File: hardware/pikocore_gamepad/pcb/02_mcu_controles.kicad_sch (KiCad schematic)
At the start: 20 parts, among them J4 LCD_FPC, Q1 2N7002, SW1 DPAD_UP, SW10 BTN_R, SW11 BTN_START, SW12 BTN_SELECT, SW2 DPAD_DOWN, SW3 DPAD_LEFT, SW4 DPAD_RIGHT, SW5 BTN_X, SW6 BTN_Y, SW7 BTN_A, SW8 BTN_B, SW9 BTN_L, U1 RP2350-Plus-16MB

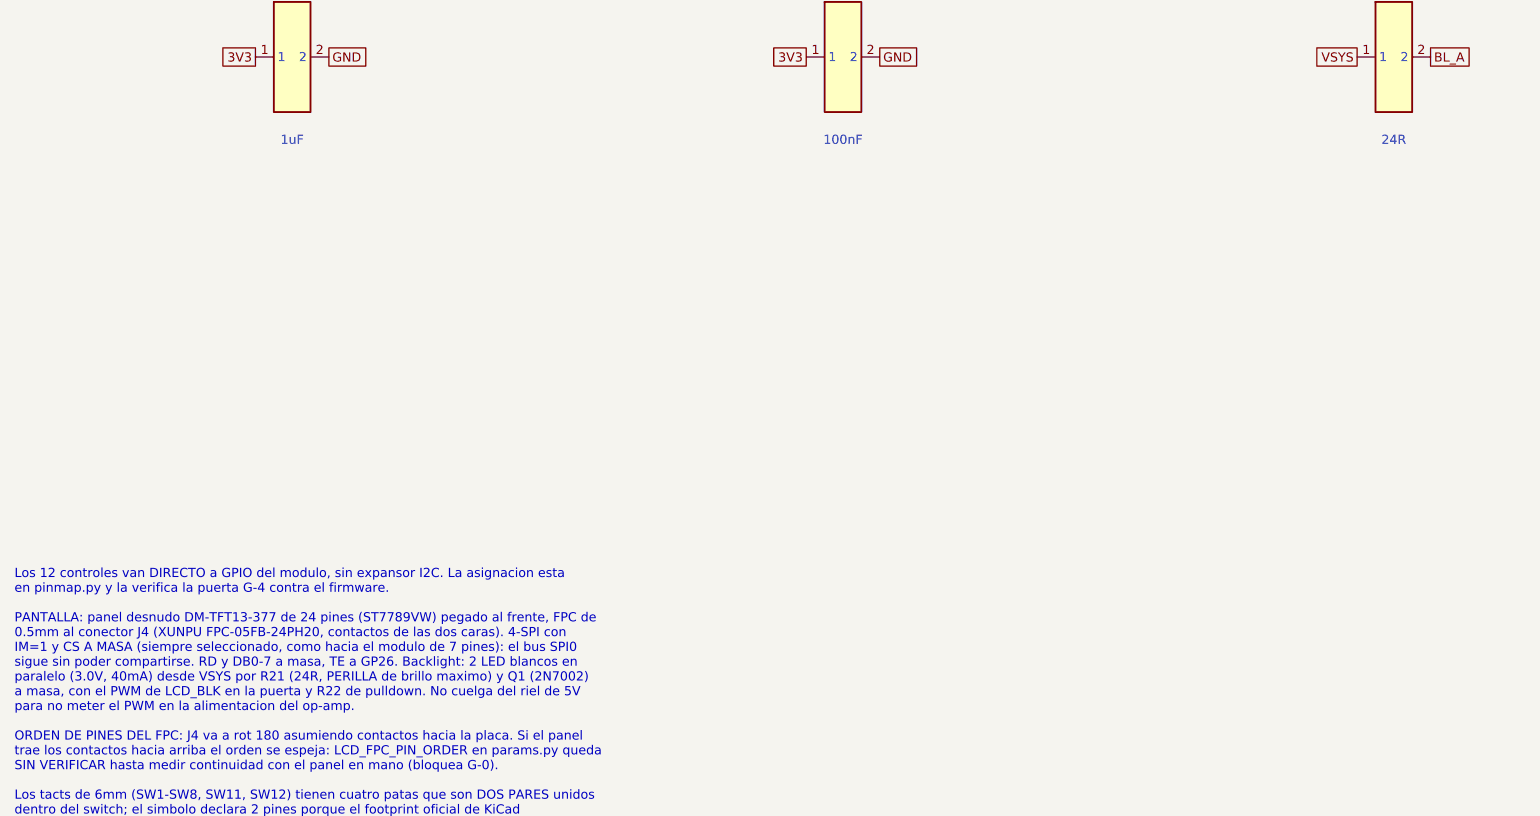
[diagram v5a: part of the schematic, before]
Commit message: hw: R21 pasa de 24R (C17576 sin stock en JLC) a 27R (C17594)
El backlight queda en 15/33/44 mA con la LiPo vacia/nominal/llena. Solo cambia
valor y codigo LCSC; el cobre no se toca (DRC 0/0/0, paridad 0).

Co-Authored-By: Claude Sonnet 5.5 <noreply@anthropic.com>
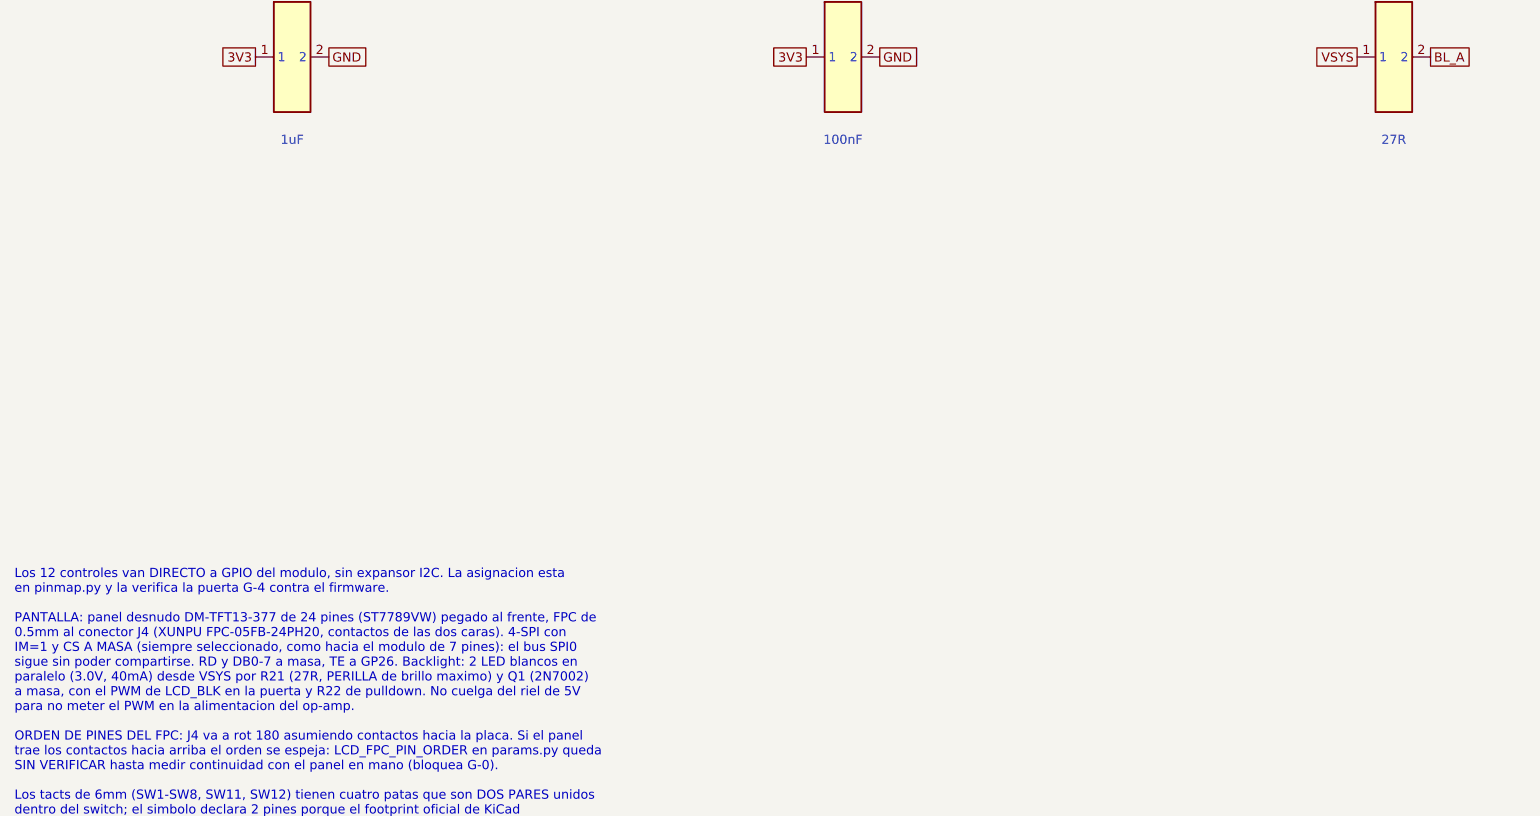
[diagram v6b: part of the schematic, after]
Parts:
- R21: value 24R -> 27R; LCSC (none) -> C17594
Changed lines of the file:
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@@
     (exclude_from_sim no) (in_bom yes) (on_board yes) (dnp no)
     (property "Reference" "R21" (at 210.82 397.51 0) (effects (font (size 1.27 1.27))))
-    (property "Value" "24R" (at 210.82 420.37 0) (effects (font (size 1.27 1.27))))
+    (property "Value" "27R" (at 210.82 420.37 0) (effects (font (size 1.27 1.27))))
     (property "Footprint" "Capacitor_SMD:C_0805_2012Metric" (at 210.82 408.94 0) (effects (font (size 1.27 1.27)) (hide yes)))
     (property "Datasheet" "" (at 210.82 408.94 0) (effects (font (size 1.27 1.27)) (hide yes)))
     (property "Description" "Resistencia SMD 0603" (at 210.82 408.94 0) (effects (font (size 1.27 1.27)) (hide yes)))
+    (property "LCSC" "C17594" (at 210.82 408.94 0) (effects (font (size 1.27 1.27)) (hide yes)))
     (pin "1")
     (pin "2")
@@
     (property "Intersheetrefs" "${INTERSHEET_REFS}" (at 292.1 408.94 0) (effects (font (size 1.27 1.27)) (hide yes)))
   )
-  (text "Los 12 controles van DIRECTO a GPIO del modulo, sin expansor I2C. La asignacion esta\nen pinmap.py y la verifica la puerta G-4 contra el firmware.\n\nPANTALLA: panel desnudo DM-TFT13-377 de 24 pines (ST7789VW) pegado al frente, FPC de\n0.5mm al conector J4 (XUNPU FPC-05FB-24PH20, contactos de las dos caras). 4-SPI con\nIM=1 y CS A MASA (siempre seleccionado, como hacia el modulo de 7 pines): el bus SPI0\nsigue sin poder compartirse. RD y DB0-7 a masa, TE a GP26. Backlight: 2 LED blancos en\nparalelo (3.0V, 40mA) desde VSYS por R21 (24R, PERILLA de brillo maximo) y Q1 (2N7002)\na masa, con el PWM de LCD_BLK en la puerta y R22 de pulldown. No cuelga del riel de 5V\npara no meter el PWM en la alimentacion del op-amp.\n\nORDEN DE PINES DEL FPC: J4 va a rot 180 asumiendo contactos hacia la placa. Si el panel\ntrae los contactos hacia arriba el orden se espeja: LCD_FPC_PIN_ORDER en params.py queda\nSIN VERIFICAR hasta medir continuidad con el panel en mano (bloquea G-0).\n\nLos tacts de 6mm (SW1-SW8, SW11, SW12) tienen cuatro patas que son DOS PARES unidos\ndentro del switch; el simbolo declara 2 pines porque el footprint oficial de KiCad\nnumera sus cuatro pads 1,1,2,2. Cablear 1 contra 2 ya cruza el contacto.\n\nSW9 y SW10 (gatillos) son angulados y tienen SOLO DOS patas electricas: las otras dos\nson soportes mecanicos, y en la placa son agujeros NO metalizados.\n\nEl D-pad son cuatro tacts independientes (SW1-SW4), no un nav switch de 5 vias: las\ncombinaciones del firmware (Up+Down+B+A = reset de FX, Down+Left+X+B = clock lock)\nnecesitan dos direcciones a la vez, cosa que un solo actuador no permite." (exclude_from_sim no) (at 20 479.8 0)
+  (text "Los 12 controles van DIRECTO a GPIO del modulo, sin expansor I2C. La asignacion esta\nen pinmap.py y la verifica la puerta G-4 contra el firmware.\n\nPANTALLA: panel desnudo DM-TFT13-377 de 24 pines (ST7789VW) pegado al frente, FPC de\n0.5mm al conector J4 (XUNPU FPC-05FB-24PH20, contactos de las dos caras). 4-SPI con\nIM=1 y CS A MASA (siempre seleccionado, como hacia el modulo de 7 pines): el bus SPI0\nsigue sin poder compartirse. RD y DB0-7 a masa, TE a GP26. Backlight: 2 LED blancos en\nparalelo (3.0V, 40mA) desde VSYS por R21 (27R, PERILLA de brillo maximo) y Q1 (2N7002)\na masa, con el PWM de LCD_BLK en la puerta y R22 de pulldown. No cuelga del riel de 5V\npara no meter el PWM en la alimentacion del op-amp.\n\nORDEN DE PINES DEL FPC: J4 va a rot 180 asumiendo contactos hacia la placa. Si el panel\ntrae los contactos hacia arriba el orden se espeja: LCD_FPC_PIN_ORDER en params.py queda\nSIN VERIFICAR hasta medir continuidad con el panel en mano (bloquea G-0).\n\nLos tacts de 6mm (SW1-SW8, SW11, SW12) tienen cuatro patas que son DOS PARES unidos\ndentro del switch; el simbolo declara 2 pines porque el footprint oficial de KiCad\nnumera sus cuatro pads 1,1,2,2. Cablear 1 contra 2 ya cruza el contacto.\n\nSW9 y SW10 (gatillos) son angulados y tienen SOLO DOS patas electricas: las otras dos\nson soportes mecanicos, y en la placa son agujeros NO metalizados.\n\nEl D-pad son cuatro tacts independientes (SW1-SW4), no un nav switch de 5 vias: las\ncombinaciones del firmware (Up+Down+B+A = reset de FX, Down+Left+X+B = clock lock)\nnecesitan dos direcciones a la vez, cosa que un solo actuador no permite." (exclude_from_sim no) (at 20 479.8 0)
     (effects (font (size 1.27 1.27)) (justify left top))
   )

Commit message: hw: pantalla de 7 pines en el esquema (sin FPC, backlight ni TE)
J4 pasa a ser el modulo IPS 1.3in ST7789 de 7 pines pasantes (simbolo
LCD_ST7789, huella gamesetup_fp:LCD_ST7789_240x240_7P, MANUAL, sin LCSC):
pines 1..7 = GND, 3V3, LCD_SCK, LCD_MOSI, LCD_RES, LCD_DC, LCD_BLK. Fuera
LCD1, R21, Q1, R22, C30, C31, los simbolos LCD_FPC24/LCD_PANEL/Q_NMOS y el
27R (C17594) de LCSC_PASIVOS. CS a GND y el transistor del backlight van en
el modulo; nota de la hoja 02 actualizada.

GP26 queda libre (FREE = (26,)), sin PIN_LCD_TE en config.h. Los GPIO libres
van a no_connect en vez de una etiqueta EXP_GP* de un solo extremo.

params.py: fuera PANEL_* y LCD_FPC_PIN_ORDER; entran las cotas LCD7_* del
dibujo del fabricante (verificadas) salvo LCD7_PIN_ROW_TO_EDGE (1.27) y
LCD7_PIN_DRILL (1.0), que se miden con el modulo en mano. gen_fp.py lleva la
geometria del modulo; la escritura de la huella y la colocacion son la
siguiente tarea (dos tests de footprint quedan rojos hasta entonces).

Co-Authored-By: Claude Sonnet 5.5 <noreply@anthropic.com>
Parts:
- removed C30: 1uF, Capacitor_SMD:C_0603_1608Metric, symbol pikocore_gamepad:C
- removed C31: 100nF, Capacitor_SMD:C_0603_1608Metric, symbol pikocore_gamepad:C
- removed LCD1: DM-TFT13-377-24P, gamesetup_fp:LCD_LH133T_24P, symbol pikocore_gamepad:LCD_PANEL
- removed Q1: 2N7002, Package_TO_SOT_SMD:SOT-23, symbol pikocore_gamepad:Q_NMOS
- removed R21: 27R, Capacitor_SMD:C_0805_2012Metric, symbol pikocore_gamepad:R
- removed R22: 100k, Resistor_SMD:R_0603_1608Metric, symbol pikocore_gamepad:R
- J4: value LCD_FPC -> ST7789_240x240; footprint gamesetup_lcsc:FPC-SMD_24P-P0.50_FPC-05FB-24PH20 -> gamesetup_fp:LCD_ST7789_240x240_7P; symbol pikocore_gamepad:LCD_FPC24 -> pikocore_gamepad:LCD_ST7789; LCSC C2856831 -> (none); now not fitted
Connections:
- net BL_A is gone; now on net GND: J4.1 (GND)
- net BL_K is gone; now on net 3V3: J4.2 (VCC)
- net 3V3: no longer J4.4 (VDD), J4.5 (VDDIO), J4.6 (IM)
- net GND: no longer J4.11 (RD), J4.13 (DB0), J4.14 (DB1), J4.15 (DB2), J4.16 (DB3), J4.17 (DB4), J4.18 (DB5), J4.19 (DB6), J4.20 (DB7), J4.23 (GND), J4.24 (GND), J4.25 (MP), J4.26 (MP), J4.3 (GND), J4.8 (CS)
- net LCD_BLK: now also J4.7 (BLK)
- net LCD_DC: now also J4.6 (DC); no longer J4.10 (D/C)
- net LCD_MOSI: now also J4.4 (SDA); no longer J4.12 (SDA)
- net LCD_RES: now also J4.5 (RES); no longer J4.7 (RESET)
- net LCD_SCK: now also J4.3 (SCL); no longer J4.9 (SCL)
- net LCD_TE: no longer names the net of U1.31 (GP26)
- net LCD_TE: no longer J4.21 (TE)
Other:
- note added: "Los 12 controles van DIRECTO a GPIO del modulo, sin expansor I2C. La asignacion esta en pinmap.py y la verifica la puerta G-4 contra el firmware. PANTALLA: modulo IPS 1.3in 240x240 ST7789 de 7 pines pasantes a 2.54 (J4), soldado por sus propios pines. CS esta atado a GND EN EL MODULO (siempre seleccionado): el bus SPI0 no se puede compartir. El backlight lo maneja directo LCD_BLK (PWM, GP7) sobre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"
- note removed: "Los 12 controles van DIRECTO a GPIO del modulo, sin expansor I2C. La asignacion esta en pinmap.py y la verifica la puerta G-4 contra el firmware. PANTALLA: panel desnudo DM-TFT13-377 de 24 pines (ST7789VW) pegado al frente, FPC de 0.5mm al conector J4 (XUNPU FPC-05FB-24PH20, contactos de las dos caras). 4-SPI con IM=1 y CS A MASA (siempre seleccionado, como hacia el modulo de 7 pines): el bus SPI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"
- moved on the sheet: U1
